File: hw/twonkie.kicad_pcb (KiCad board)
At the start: 4 copper layers, 25.4 x 25.4 mm, 59 parts, among them J1 USB4151, J2 690-024-294T331, J3 629105150521, Q1 BSD840N, Q2 BSD840N, Q3 BSD840N, Q4 BSD840N, SW1 EVQ-P7M01P, U1 INA260, U2 INA260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

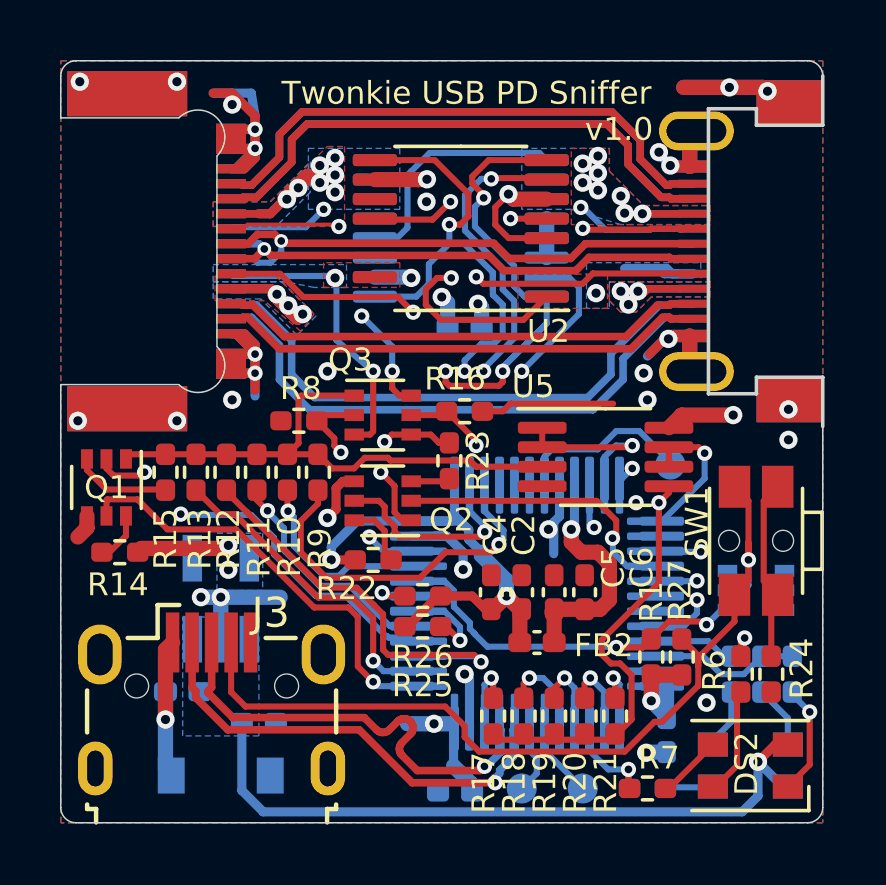
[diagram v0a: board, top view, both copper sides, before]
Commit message: Last minute fixes
 * Add back C8 which had accidentally been deleted
 * Flip Q4 source<->drain
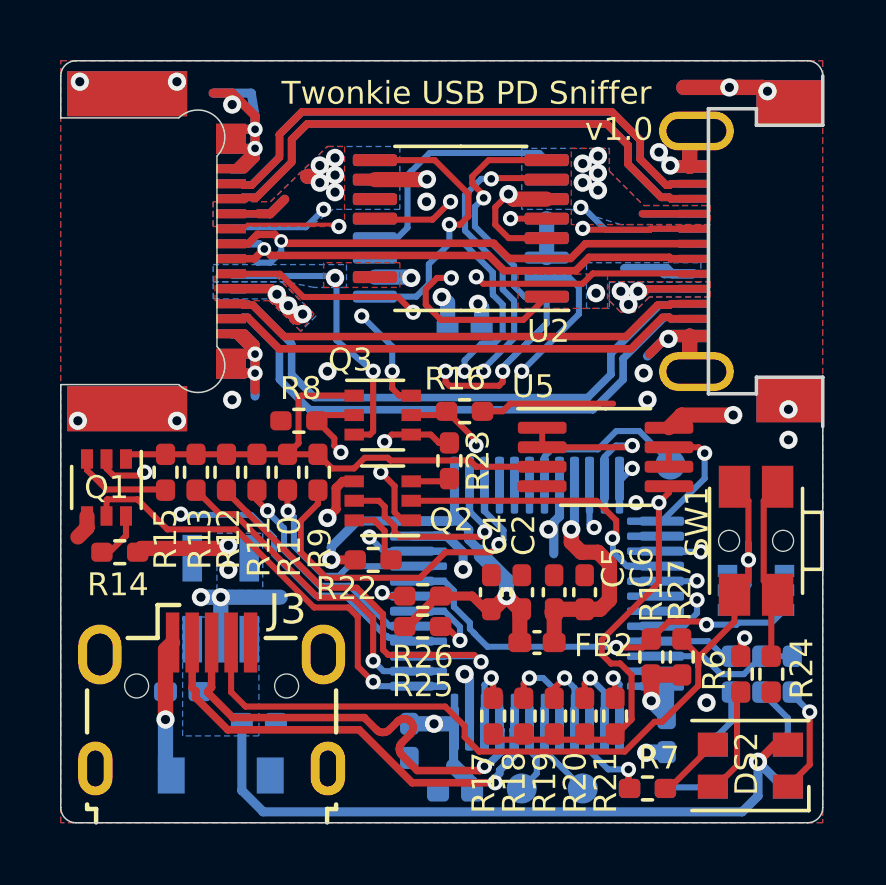
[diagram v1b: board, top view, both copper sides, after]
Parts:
- added C8: 100n, Capacitor_SMD:C_0402_1005Metric_Pad0.74x0.62mm_HandSolder, B.Cu at (83.5, 57.0)
- R2, R5: value 390 -> 620
- R3, R4, R6, R7: value 240 -> 400
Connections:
- Q4 pad 1: /BOOT -> GND
- Q4 pad 6: GND -> /BOOT
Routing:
- net /VBUS_RECEP: track 12.4 -> 10.0 mm, vias 10 -> 8
- net /BOOT: track 12.5 -> 14.4 mm
- net /VBUS_PLUG: vias 11 -> 8

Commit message: Twonkie v2.0 alpha hardware
Upgrade the project to KiCad 6.0, fixing a whole bunch of new ERC/DRC
errors and warnings.

Switch from INA260 to INA237 which supports EPR voltage ranges, with
external shunt resistors.

Strap a previously unused pin on the STM32 to indicate the board
revision, so firmware can detect which hardware it's running on.
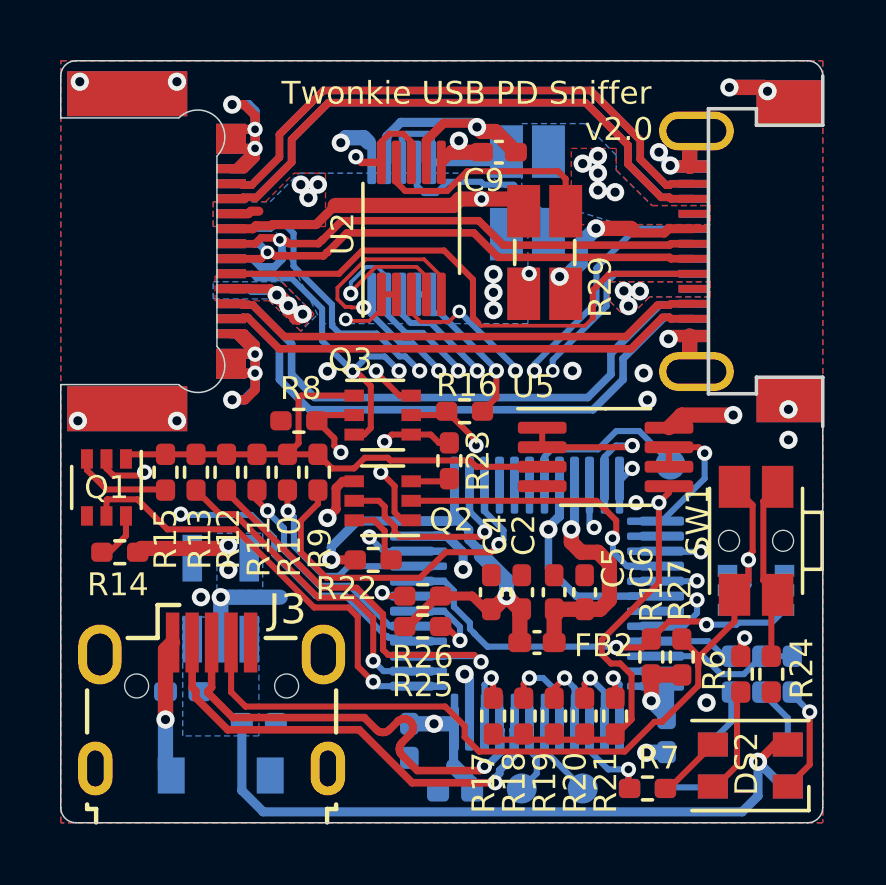
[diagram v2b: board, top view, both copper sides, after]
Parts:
- removed ?: , 
- added HEART: , , F.Cu at (78.0, 34.8)
- added R28: 0.012, Resistor_SMD:R_Shunt_Ohmite_LVK12, B.Cu at (87.4, 38.7)
- added R29: 0.012, Resistor_SMD:R_Shunt_Ohmite_LVK12, F.Cu at (88.0, 40.7)
- C9: moved to F.Cu
- U1, U2: value INA260 -> INA237; footprint Package_SO:TSSOP-16_4.4x5mm_P0.65mm -> Package_SO:VSSOP-10_3x3mm_P0.5mm
- moved C9 5.95 mm to (86.5, 37.3)
- moved U1 1.97 mm to (83.2, 39.9), turned to 90 degrees
- moved U2 1.65 mm to (83.6, 39.9), turned to 90 degrees
- moved dojoe-logo 0.32 mm to (85.2, 45.4)
- renumbered G*** to OSHW_LOGO
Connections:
- J1 pad A5: /CC1_RECEP -> /CC1_PLUG
- J1 pad B5: /CC2_PLUG -> /CC2_RECEP
- U1 pad 1: /VBUS_PLUG -> GND
- U1 pad 10: +3V3 -> /VRBUS+
- U1 pad 2: /VBUS_PLUG -> GND
- U1 pad 3: /VBUS_PLUG -> /VBUS_ALERT_L
- U1 pad 4: GND -> /INA_SDA
- U1 pad 5: GND -> /INA_SCL
- U1 pad 6: GND -> +3V3
- U1 pad 7: /VBUS_ALERT_L -> GND
- U1 pad 8: /INA_SDA -> /VRBUS+
- U1 pad 9: /INA_SCL -> /VRBUS-
- U2 pad 1: /CC2_PLUG -> +3V3
- U2 pad 10: +3V3 -> /VRCONN+
- U2 pad 4: GND -> /INA_SDA
- U2 pad 5: +3V3 -> /INA_SCL
- U2 pad 6: GND -> +3V3
- U2 pad 7: /VCONN_ALERT_L -> GND
- U2 pad 8: /INA_SDA -> /VRCONN+
- U2 pad 9: /INA_SCL -> /VRCONN-
- U3 pad 4: Net-(U3-Pad4) -> unconnected-(U3-Pad4)
- U4 pad 18: Net-(U4-Pad18) -> GND
- U4 pad 19: Net-(U4-Pad19) -> unconnected-(U4-Pad19)
- U4 pad 4: Net-(U4-Pad4) -> unconnected-(U4-Pad4)
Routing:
- net /CC2_PLUG: track 16.4 -> 0.00 mm, vias 3 -> 0
- net /CC2_RECEP: track 9.94 -> 23.8 mm, vias 2 -> 3
- net +3V3: track 45.6 -> 59.5 mm
- net /VBUS_PLUG: track 12.9 -> 0.00 mm
- net /VRCONN+: track 0.00 -> 11.0 mm, vias 0 -> 2
- net /VRCONN-: track 0.00 -> 7.88 mm
- net /INA_SDA: track 26.6 -> 19.1 mm, vias 4 -> 3
- net /VCONN_ALERT_L: track 21.5 -> 15.4 mm
- net /VRBUS-: track 0.00 -> 5.94 mm
- net /INA_SCL: track 30.6 -> 25.0 mm
- net /CC1_PLUG: track 0.00 -> 5.57 mm, vias 0 -> 2
- net /VRBUS+: track 0.00 -> 4.93 mm
- net /SBU2: track 17.2 -> 22.1 mm
- net /VBUS_RECEP: track 10.0 -> 6.81 mm, vias 8 -> 9
- net GND: track 64.0 -> 60.9 mm, vias 31 -> 30
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- removed copper zone on In2.Cu, net +3V3
- removed copper zone on B.Cu, net /CC2_PLUG
- removed copper zone on F.Cu, net /CC2_PLUG
- removed copper zone on B.Cu, net /CC2_RECEP
- removed copper zone on F.Cu, net /CC2_RECEP
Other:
- net class Default removed
- net class Diffpair removed
- net class Power removed
- board text added: "2023"
- board text added: "v2.0"
- board text removed: "2020"
- board text removed: "v1.0"

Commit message: v2.0: Updates based on David's review
* Wire sense resistors according to datasheet (measured current flows
  along a long edge instead of diagonally)
* Rotate R28 and move C9 to allow for that, this also unclutters the
  vias and traces around the INA237 north sides and improves copper
  plane shape
* Connect inner VBUS shape to upper via group too
* Give the RX2 pair a little more breathing room

Thanks @dnschneid for the review! <3 (see #4)
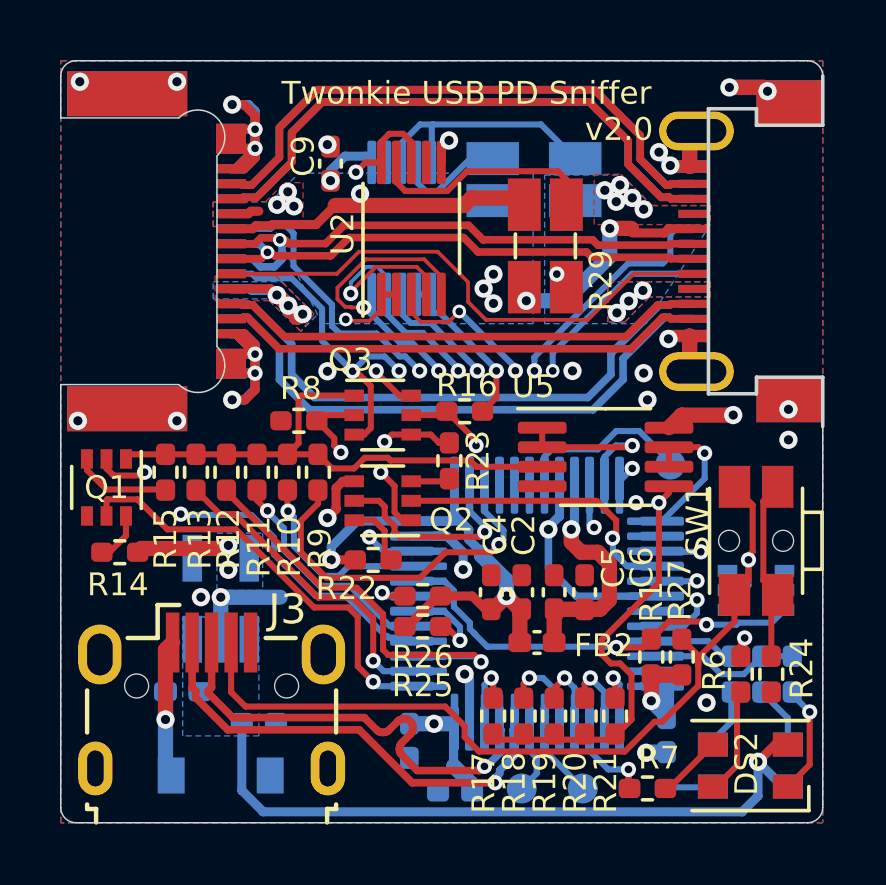
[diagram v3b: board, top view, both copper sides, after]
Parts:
- R28, R29: footprint Resistor_SMD:R_Shunt_Ohmite_LVK12 -> twonkie:R_Shunt_Ohmite_LVK12
- moved C9 5.63 mm to (80.9, 37.7), turned to 90 degrees
- moved R28 0.49 mm to (87.7, 38.3), turned to -90 degrees
- moved R29 0.22 mm to (88.0, 40.5)
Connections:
- R28 pad 1: /VBUS_PLUG -> /VBUS_RECEP
- R28 pad 2: /VRBUS+ -> /VRBUS-
- R28 pad 3: /VRBUS- -> /VRBUS+
- R28 pad 4: /VBUS_RECEP -> /VBUS_PLUG
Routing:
- net GND: track 60.9 -> 52.6 mm
- net /CC1_RECEP: track 23.1 -> 29.2 mm
- net /VRBUS+: track 4.93 -> 8.44 mm
- net /VRBUS-: track 5.94 -> 3.76 mm
- net /CC1_PLUG: track 5.57 -> 7.15 mm
- net /VRCONN+: track 11.0 -> 12.4 mm
- net /SBU1: track 18.8 -> 17.7 mm

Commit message: hw: Move TP1 a bit so it doesn't look like a pin 1 marker (ask me how i know)
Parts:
- moved TP1 1.16 mm to (92.0, 46.6)
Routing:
- net /NRST: track 5.72 -> 5.12 mm
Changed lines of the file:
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@@
   )
   (footprint "TestPoint:TestPoint_Pad_D1.0mm" (layer "B.Cu")
-    (at 92.202 47.752)
+    (at 92.0242 46.609)
     (descr "SMD pad as test Point, diameter 1.0mm")
     (tags "test point SMD pad")
@@
     (property "exclude_from_bom" "")
     (attr exclude_from_pos_files exclude_from_bom)
-    (fp_text reference "TP1" (at 0.254 -1.27) (layer "B.SilkS")
+    (fp_text reference "TP1" (at 0.0762 1.4986 180) (layer "B.SilkS")
       (effects (font (size 0.762 0.762) (thickness 0.127)) (justify mirror))
     )
@@
   (segment (start 87.507 56.55) (end 87.507 57.2875) (width 0.2032) (layer "B.Cu") (net 40))
   (segment (start 87.748999 57.529499) (end 87.748999 58.047001) (width 0.2032) (layer "B.Cu") (net 40))
-  (segment (start 91.163649 46.634399) (end 92.202 47.67275) (width 0.2032) (layer "B.Cu") (net 41))
   (segment (start 88.007 48.225) (end 88.007 47.4875) (width 0.2032) (layer "B.Cu") (net 41))
-  (segment (start 90.398602 46.634399) (end 91.163649 46.634399) (width 0.2032) (layer "B.Cu") (net 41))
-  (segment (start 89.789001 47.244) (end 90.398602 46.634399) (width 0.2032) (layer "B.Cu") (net 41))
-  (segment (start 88.2505 47.244) (end 89.789001 47.244) (width 0.2032) (layer "B.Cu") (net 41))
+  (segment (start 90.17 46.863) (end 90.424 46.609) (width 0.2032) (layer "B.Cu") (net 41))
+  (segment (start 90.424 46.609) (end 92.0242 46.609) (width 0.2032) (layer "B.Cu") (net 41))
   (segment (start 88.007 47.4875) (end 88.2505 47.244) (width 0.2032) (layer "B.Cu") (net 41))
+  (segment (start 89.789014 47.244) (end 90.17 46.863014) (width 0.2032) (layer "B.Cu") (net 41))
+  (segment (start 90.17 46.863014) (end 90.17 46.863) (width 0.2032) (layer "B.Cu") (net 41))
+  (segment (start 88.2505 47.244) (end 89.789014 47.244) (width 0.2032) (layer "B.Cu") (net 41))
   (segment (start 81.555697 42.4942) (end 81.364989 42.4942) (width 0.127) (layer "F.Cu") (net 42))
   (segment (start 81.104607 42.233818) (end 81.104607 41.856793) (width 0.127) (layer "F.Cu") (net 42))
